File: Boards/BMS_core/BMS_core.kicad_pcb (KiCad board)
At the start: 2 copper layers, 73.7 x 61 mm, 67 parts, among them IC1 ATMEGA16M1, J1 CONN_02X03, J2 B5B-PH-K-S, J3 NanoFit_2, J4 MicroFit_RA_R_2, J5 MM_F_VT_14, K1 G5Q-1A4-DC5-5V, Q1 SSM3K333R, T1 T_LAN_7490100111A, U1 MCP2561-E_SN, U101 TPS561201, U2 SN74LVC1G17, U3 LTC6820HMS, U4 MCP6001, U5 MCP6001, Y1 Crystal_SMD

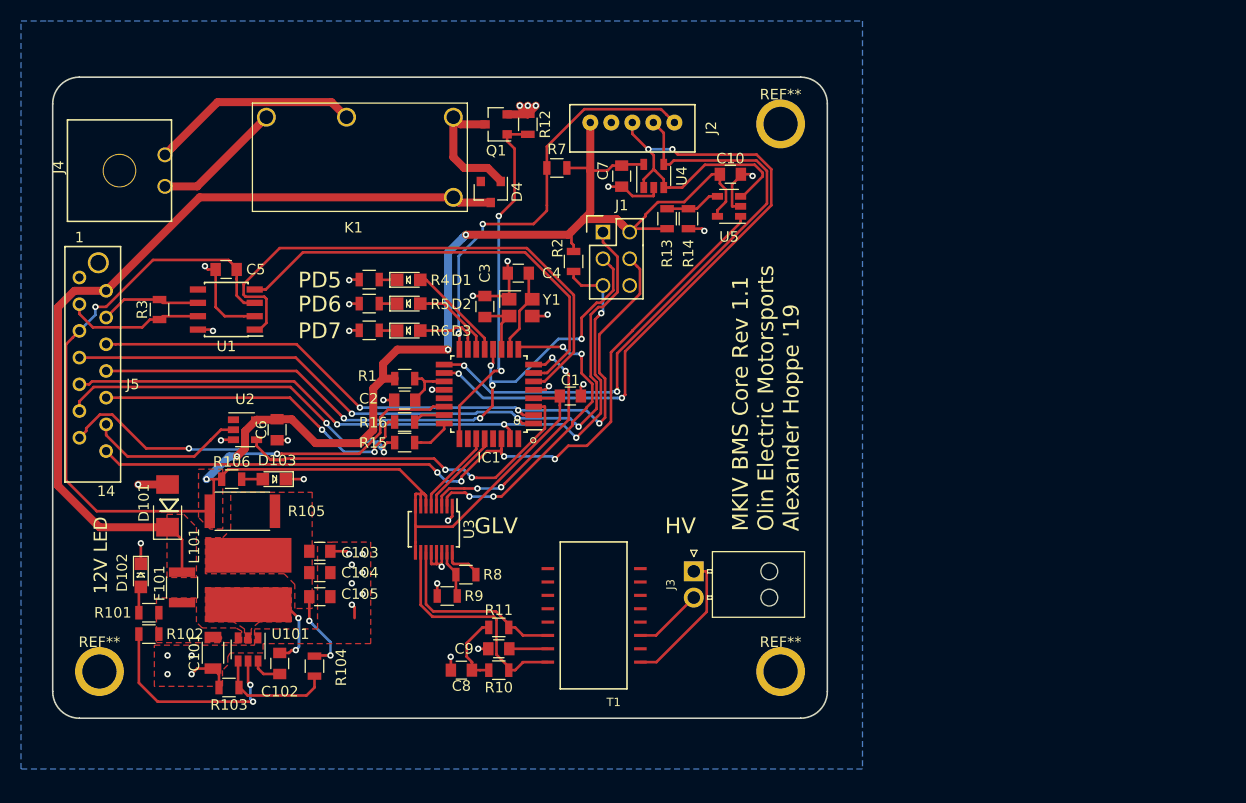
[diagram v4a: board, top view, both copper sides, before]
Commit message: Edit BMS_core for rev 1.2, couple of small fixes
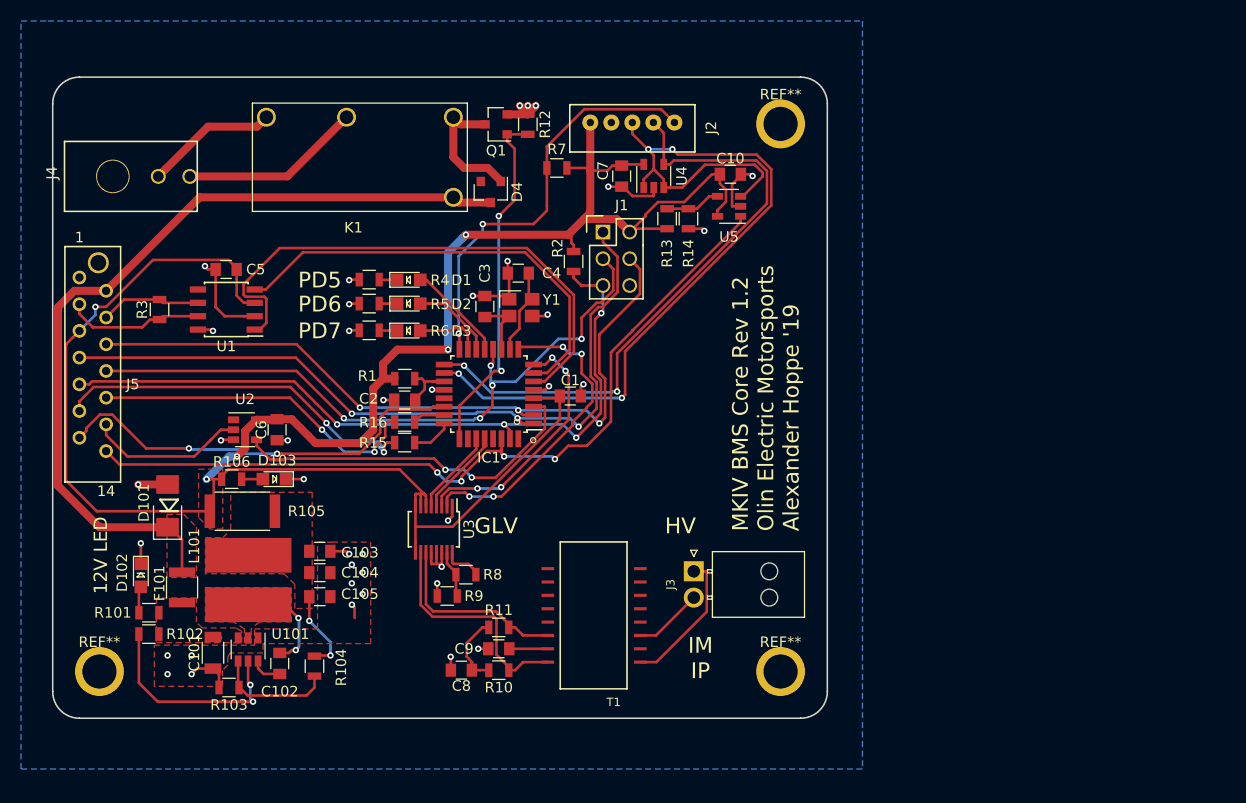
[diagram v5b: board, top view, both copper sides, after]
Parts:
- J4: value MicroFit_RA_R_2 -> MicroFit_RA_V_2; footprint footprints:MicroFit_RA_2 -> footprints:MicroFit_RA_V_2
- moved J4 0.84 mm to (48.9, 57.7)
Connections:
- U3 pad 12: GND -> VCC
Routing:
- net /SHDN_OUT(BMS->IMD): track 19.9 -> 17.2 mm
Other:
- board text added: "IM IP"
- board text added: "MKIV BMS Core Rev 1.2 Olin Electric Motorsports Alexander Hoppe '19"
- board text removed: "MKIV BMS Core Rev 1.1 Olin Electric Motorsports Alexander Hoppe '19"
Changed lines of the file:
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@@
   (general
     (thickness 1.6)
-    (drawings 16)
+    (drawings 17)
     (tracks 769)
     (zones 0)
@@
   )
   (setup
-    (last_trace_width 0.254)
+    (last_trace_width 0.762)
     (user_trace_width 0.1524)
     (user_trace_width 0.254)
@@
     )
   )
-  (module footprints:MicroFit_RA_2 (layer F.Cu)
-    (at 49.53 57.15 90)
-    (fp_text reference J4 (at 0.3302 -5.7912 90) (layer F.SilkS)
-      (effects (font (size 1 1) (thickness 0.15)))
-    )
-    (fp_text value MicroFit_RA_R_2 (at 0.254 6.0452 90) (layer F.Fab)
-      (effects (font (size 1 1) (thickness 0.15)))
-    )
-    (fp_line (start 4.825 -4.95) (end 4.825 4.95) (layer F.SilkS) (width 0.15))
-    (fp_line (start -4.825 -4.95) (end -4.825 4.95) (layer F.SilkS) (width 0.15))
-    (fp_line (start -4.825 -4.95) (end 4.825 -4.95) (layer F.SilkS) (width 0.15))
-    (fp_line (start -4.825 4.95) (end 4.825 4.95) (layer F.SilkS) (width 0.15))
-    (pad "" thru_hole circle (at 0 0 90) (size 3.2 3.2) (drill 3) (layers *.Cu *.Mask))
-    (pad 1 thru_hole circle (at -1.5 4.32 90) (size 1.42 1.42) (drill 1.02) (layers *.Cu *.Mask)
-      (net 57 "/SHDN_IN(MAIN_PACK->BMS)"))
-    (pad 2 thru_hole circle (at 1.5 4.32 90) (size 1.42 1.42) (drill 1.02) (layers *.Cu *.Mask)
-      (net 58 "/SHDN_OUT(BMS->IMD)"))
-  )
   (module footprints:micromatch_female_vert_14 (layer F.Cu)
     (at 45.72 72.39)
@@
       (net 52 /CS_iso))
     (pad 12 smd rect (at 2.2 0.25 270) (size 1.4 0.3) (layers F.Cu F.Paste F.Mask)
-      (net 1 GND))
+      (net 2 VCC))
     (pad 13 smd rect (at 2.2 -0.25 270) (size 1.4 0.3) (layers F.Cu F.Paste F.Mask)
       (net 1 GND))
@@
     )
   )
+  (module footprints:MicroFit_RA_V_2 (layer F.Cu)
+    (at 48.9 57.7 90)
+    (fp_text reference J4 (at 0.3302 -5.7912 90) (layer F.SilkS)
+      (effects (font (size 1 1) (thickness 0.15)))
+    )
+    (fp_text value MicroFit_RA_V_2 (at -2.3876 1.5494 180) (layer F.Fab)
+      (effects (font (size 1 1) (thickness 0.15)))
+    )
+    (fp_line (start 3.325 8) (end 3.325 -4.6) (layer F.SilkS) (width 0.15))
+    (fp_line (start -3.325 -4.6) (end -3.325 8) (layer F.SilkS) (width 0.15))
+    (fp_line (start -3.3274 -4.5974) (end 3.3274 -4.5974) (layer F.SilkS) (width 0.15))
+    (fp_line (start -3.3274 8.0264) (end 3.3274 8.0264) (layer F.SilkS) (width 0.15))
+    (pad "" thru_hole circle (at 0 0 90) (size 3.2 3.2) (drill 3) (layers *.Cu *.Mask))
+    (pad 1 thru_hole circle (at 0 4.32 90) (size 1.42 1.42) (drill 1.02) (layers *.Cu *.Mask)
+      (net 57 "/SHDN_IN(MAIN_PACK->BMS)"))
+    (pad 2 thru_hole circle (at 0 7.32 90) (size 1.42 1.42) (drill 1.02) (layers *.Cu *.Mask)
+      (net 58 "/SHDN_OUT(BMS->IMD)"))
+  )
+  (gr_text "IM\nIP" (at 104.775 103.505) (layer F.SilkS)
+    (effects (font (size 1.5 1.5) (thickness 0.3)))
+  )
   (gr_arc (start 45.72 106.68) (end 43.18 106.68) (angle -90) (layer Edge.Cuts) (width 0.15))
   (gr_arc (start 114.3 106.68) (end 114.3 109.22) (angle -90) (layer Edge.Cuts) (width 0.15))
@@
   (gr_line (start 116.84 50.8) (end 116.84 106.68) (layer Edge.Cuts) (width 0.15))
   (gr_line (start 45.72 48.26) (end 114.3 48.26) (layer Edge.Cuts) (width 0.15))
-  (gr_text "MKIV BMS Core Rev 1.1\nOlin Electric Motorsports\nAlexander Hoppe '19" (at 110.998 91.44 90) (layer F.SilkS)
+  (gr_text "MKIV BMS Core Rev 1.2\nOlin Electric Motorsports\nAlexander Hoppe '19" (at 110.998 91.44 90) (layer F.SilkS)
     (effects (font (size 1.5 1.5) (thickness 0.3)) (justify left))
   )
@@
   (segment (start 100.544 101.346) (end 99.06 101.346) (width 0.254) (layer F.Cu) (net 56))
   (segment (start 104.14 97.75) (end 100.544 101.346) (width 0.254) (layer F.Cu) (net 56))
-  (segment (start 56.92 58.65) (end 53.85 58.65) (width 0.762) (layer F.Cu) (net 57))
-  (segment (start 63.5 52.07) (end 56.92 58.65) (width 0.762) (layer F.Cu) (net 57))
-  (segment (start 54.559999 54.940001) (end 53.85 55.65) (width 0.762) (layer F.Cu) (net 58))
-  (segment (start 58.863401 50.636599) (end 54.559999 54.940001) (width 0.762) (layer F.Cu) (net 58))
-  (segment (start 69.686599 50.636599) (end 58.863401 50.636599) (width 0.762) (layer F.Cu) (net 58))
-  (segment (start 71.12 52.07) (end 69.686599 50.636599) (width 0.762) (layer F.Cu) (net 58))
+  (segment (start 53.929999 56.990001) (end 53.22 57.7) (width 0.762) (layer F.Cu) (net 57))
+  (segment (start 57.950001 52.969999) (end 53.929999 56.990001) (width 0.762) (layer F.Cu) (net 57))
+  (segment (start 62.600001 52.969999) (end 57.950001 52.969999) (width 0.762) (layer F.Cu) (net 57))
+  (segment (start 63.5 52.07) (end 62.600001 52.969999) (width 0.762) (layer F.Cu) (net 57))
+  (segment (start 65.49 57.7) (end 71.12 52.07) (width 0.762) (layer F.Cu) (net 58))
+  (segment (start 56.22 57.7) (end 65.49 57.7) (width 0.762) (layer F.Cu) (net 58))
   (segment (start 75.093 81.0514) (end 74.803 81.3414) (width 0.254) (layer F.Cu) (net 59))
   (segment (start 75.697 81.0514) (end 75.093 81.0514) (width 0.254) (layer F.Cu) (net 59))

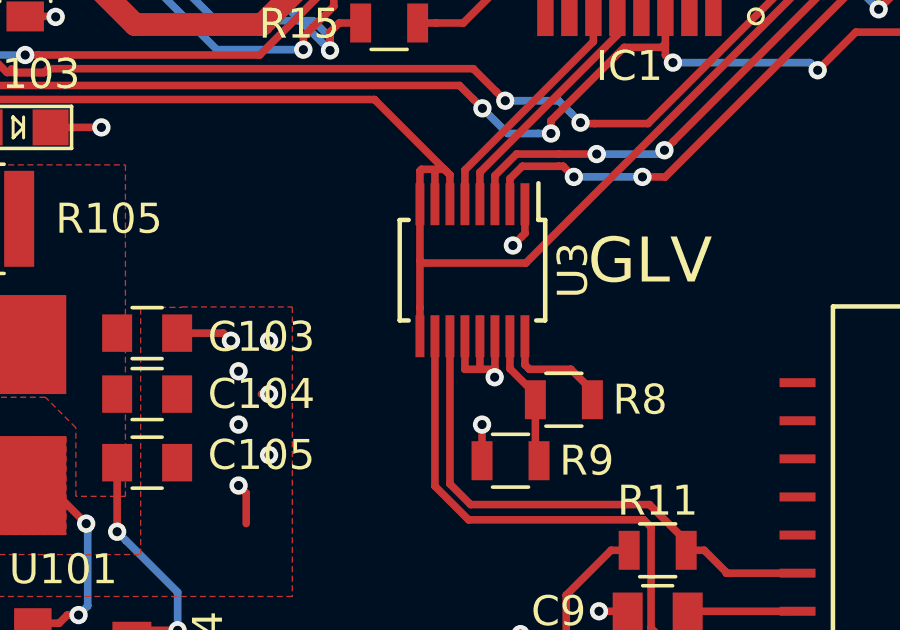
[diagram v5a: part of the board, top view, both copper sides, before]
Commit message: Fix ltc6820 connection, thanks DRC!
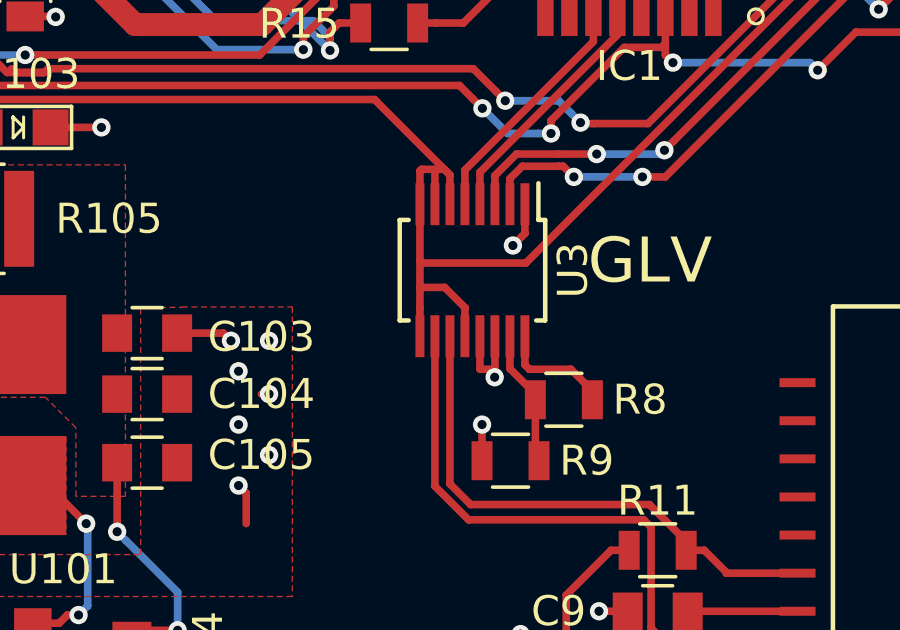
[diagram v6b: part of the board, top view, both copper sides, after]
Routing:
- net VCC: track 211.6 -> 214.3 mm
- net GND: track 70.8 -> 69.1 mm
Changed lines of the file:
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@@
     (thickness 1.6)
     (drawings 17)
-    (tracks 769)
+    (tracks 770)
     (zones 0)
     (modules 67)
@@
   )
   (setup
-    (last_trace_width 0.762)
+    (last_trace_width 0.254)
     (user_trace_width 0.1524)
     (user_trace_width 0.254)
@@
   (segment (start 79.673511 94.545383) (end 79.673511 93.447383) (width 0.254) (layer F.Cu) (net 1))
   (segment (start 79.677511 94.549383) (end 79.673511 94.545383) (width 0.254) (layer F.Cu) (net 1))
-  (segment (start 79.677511 94.549383) (end 79.169511 94.549383) (width 0.254) (layer F.Cu) (net 1))
-  (segment (start 79.173511 94.545383) (end 79.173511 93.447383) (width 0.254) (layer F.Cu) (net 1))
-  (segment (start 79.169511 94.549383) (end 79.173511 94.545383) (width 0.254) (layer F.Cu) (net 1))
   (via (at 80.164105 94.815402) (size 0.6096) (drill 0.3048) (layers F.Cu B.Cu) (net 1))
   (segment (start 80.161511 94.812808) (end 80.164105 94.815402) (width 0.254) (layer F.Cu) (net 1))
@@
   (segment (start 77.724 87.884) (end 77.673511 87.934489) (width 0.254) (layer F.Cu) (net 2))
   (segment (start 77.673511 93.447383) (end 77.673511 92.493383) (width 0.254) (layer F.Cu) (net 2))
-  (segment (start 77.673511 92.493383) (end 77.673511 90.932) (width 0.254) (layer F.Cu) (net 2))
   (segment (start 77.673511 90.932) (end 77.673511 89.047383) (width 0.254) (layer F.Cu) (net 2))
   (segment (start 60.674 69.036) (end 60.674 67.427) (width 0.254) (layer F.Cu) (net 2))
@@
   (segment (start 73.66 81.8134) (end 73.66 77.863999) (width 0.762) (layer F.Cu) (net 2))
   (segment (start 64.516 80.788) (end 65.903 80.788) (width 0.762) (layer F.Cu) (net 2))
+  (segment (start 78.501128 91.821) (end 77.673511 91.821) (width 0.254) (layer F.Cu) (net 2))
+  (segment (start 79.173511 92.493383) (end 78.501128 91.821) (width 0.254) (layer F.Cu) (net 2))
+  (segment (start 79.173511 93.447383) (end 79.173511 92.493383) (width 0.254) (layer F.Cu) (net 2))
+  (segment (start 77.673511 92.493383) (end 77.673511 91.821) (width 0.254) (layer F.Cu) (net 2))
+  (segment (start 77.673511 91.821) (end 77.673511 90.932) (width 0.254) (layer F.Cu) (net 2))
   (via (at 71.628 80.264) (size 0.6096) (drill 0.3048) (layers F.Cu B.Cu) (net 3))
   (segment (start 71.628 80.264) (end 66.294 74.93) (width 0.254) (layer F.Cu) (net 3))

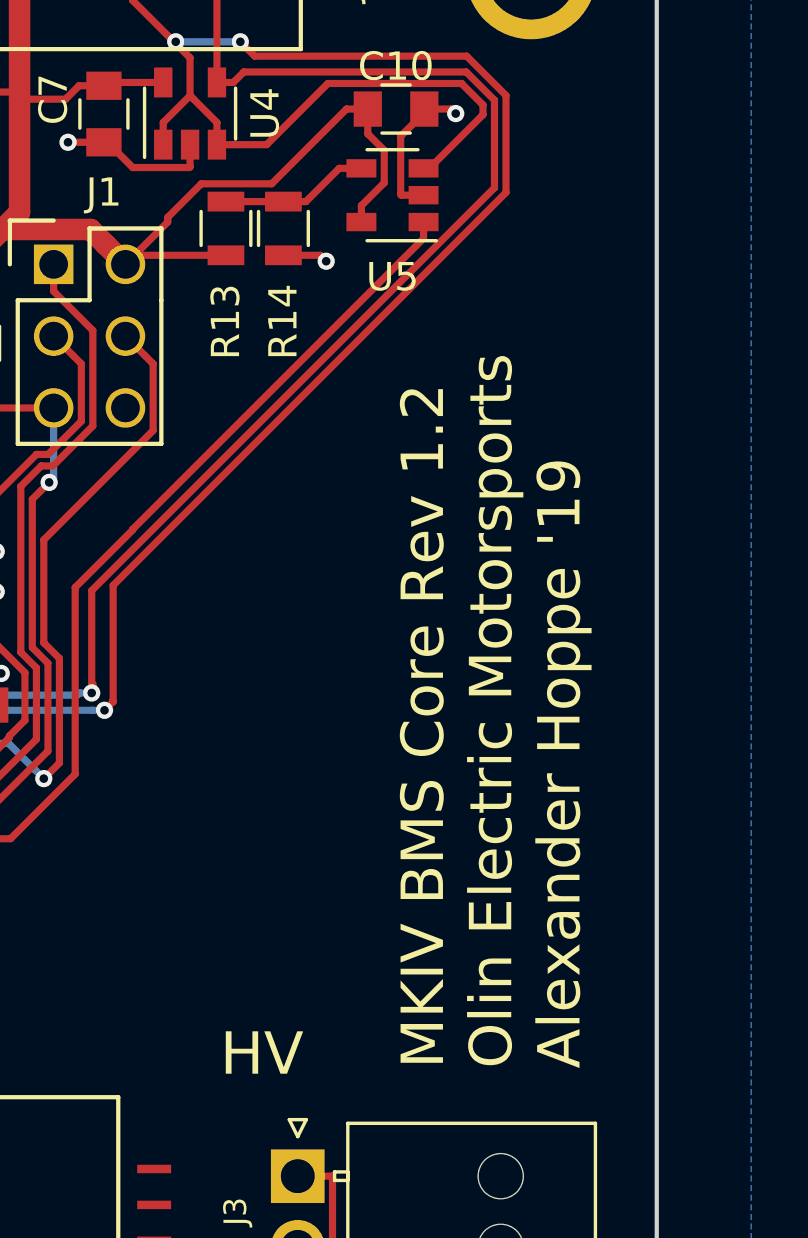
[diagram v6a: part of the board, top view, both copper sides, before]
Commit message: Add BMS_core rev 1.3 with plane cutout for HV area
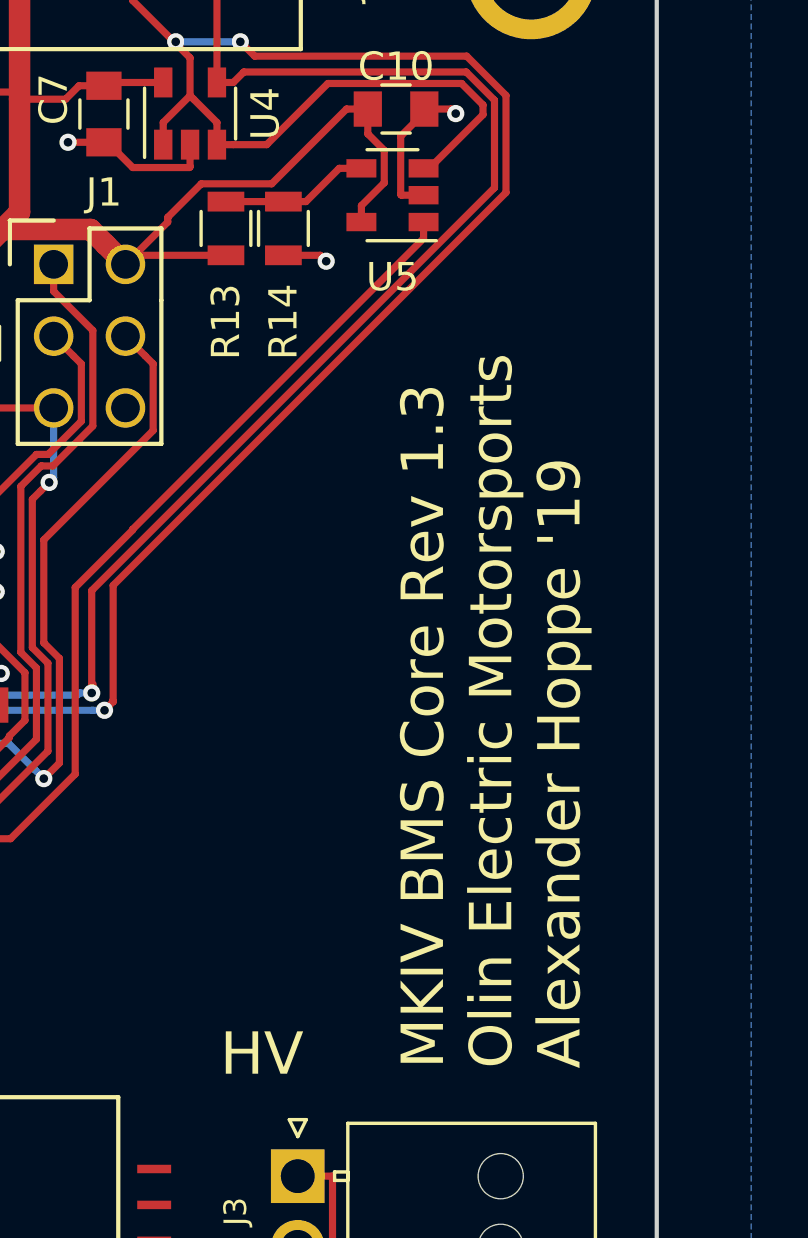
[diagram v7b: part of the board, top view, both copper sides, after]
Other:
- board text added: "MKIV BMS Core Rev 1.3 Olin Electric Motorsports Alexander Hoppe '19"
- board text removed: "MKIV BMS Core Rev 1.2 Olin Electric Motorsports Alexander Hoppe '19"
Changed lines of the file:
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@@
   )
   (setup
-    (last_trace_width 0.254)
+    (last_trace_width 0.1524)
     (user_trace_width 0.1524)
     (user_trace_width 0.254)
@@
   (gr_line (start 116.84 50.8) (end 116.84 106.68) (layer Edge.Cuts) (width 0.15))
   (gr_line (start 45.72 48.26) (end 114.3 48.26) (layer Edge.Cuts) (width 0.15))
-  (gr_text "MKIV BMS Core Rev 1.2\nOlin Electric Motorsports\nAlexander Hoppe '19" (at 110.998 91.44 90) (layer F.SilkS)
+  (gr_text "MKIV BMS Core Rev 1.3\nOlin Electric Motorsports\nAlexander Hoppe '19" (at 110.998 91.44 90) (layer F.SilkS)
     (effects (font (size 1.5 1.5) (thickness 0.3)) (justify left))
   )
@@
       )
     )
+  )
+  (zone (net 0) (net_name "") (layer B.Cu) (hatch edge 0.508)
+    (connect_pads (clearance 0.1524))
+    (min_thickness 0.254)
+    (keepout (tracks allowed) (vias allowed) (copperpour not_allowed))
+    (fill (arc_segments 16) (thermal_gap 0.508) (thermal_bridge_width 0.508))
+    (polygon
+      (pts
+        (xy 88.011 109.347) (xy 88.011 86.614) (xy 89.281 85.344) (xy 92.075 85.344) (xy 99.06 78.359)
+        (xy 117.729 78.359) (xy 117.729 109.22) (xy 117.729 109.347)
+      )
+    )
